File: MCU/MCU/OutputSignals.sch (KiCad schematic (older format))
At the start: 31 parts, among them J11 Conn_01x02, J12 Conn_01x02, J13 Conn_01x02, Q2 8050, Q3 8050, Q4 8550, Q5 8050, U10 LMV321, U11 PC817, U9 ICL7660

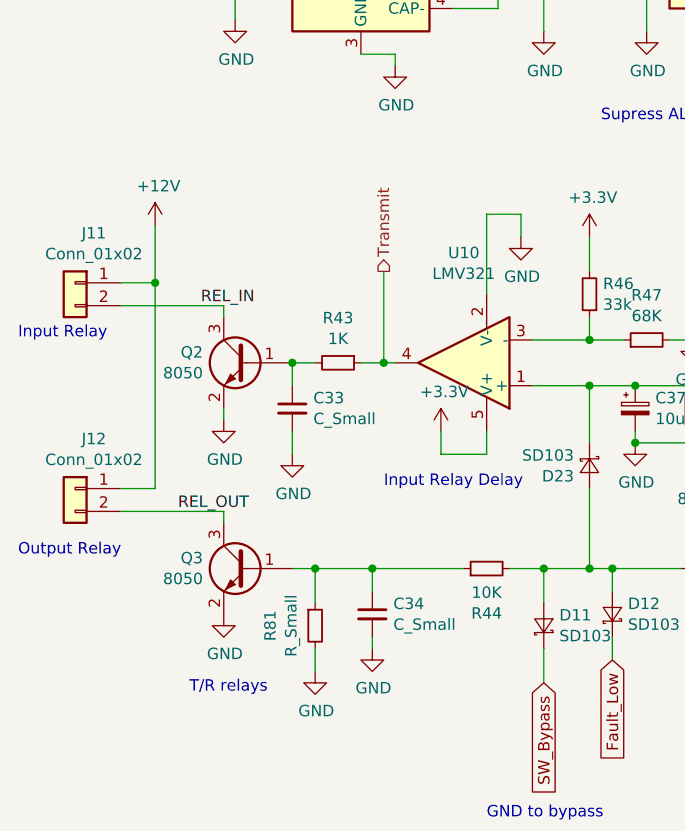
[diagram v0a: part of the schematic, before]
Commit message: OPA1000 and 2000 compatibility
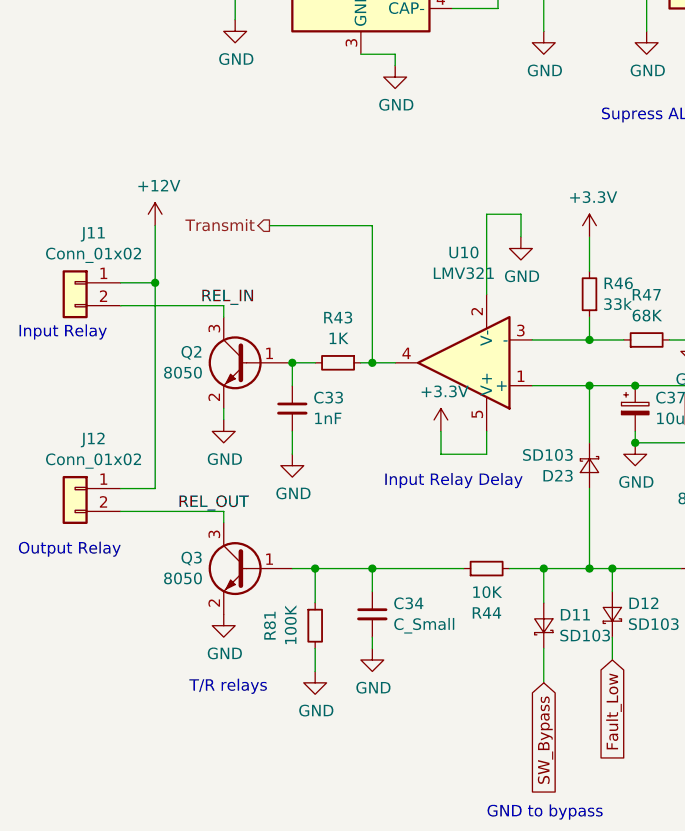
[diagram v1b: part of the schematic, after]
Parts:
- C33: value C_Small -> 1nF
- R81: value R_Small -> 100K
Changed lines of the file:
@@
 EESchema Schematic File Version 4
-LIBS:MCU-cache
 EELAYER 30 0
 EELAYER END
@@
 Text HLabel 4900 2450 3    50   Input ~ 0
 ALC_trig
-Text HLabel 2850 2850 1    50   Output ~ 0
-Transmit
 Text Notes 1250 4100 0    50   ~ 0
 Output Relay
@@
 	4100 3150 4200 3150
 Wire Wire Line
-	2850 2850 2850 3250
-Wire Wire Line
-	2850 3250 2900 3250
-Wire Wire Line
 	2450 4150 2550 4150
 Wire Wire Line
@@
 $EndComp
 Wire Wire Line
-	2750 3250 2850 3250
-Connection ~ 2850 3250
-Wire Wire Line
 	2550 3250 2450 3250
 $Comp
@@
 P 2450 3450
 F 0 "C33" H 2542 3496 50  0000 L CNN
-F 1 "C_Small" H 2542 3405 50  0000 L CNN
+F 1 "1nF" H 2542 3405 50  0000 L CNN
 F 2 "Capacitors_SMD:C_0805" H 2450 3450 50  0001 C CNN
 F 3 "~" H 2450 3450 50  0001 C CNN
@@
 P 2550 4400
 F 0 "R81" V 2354 4400 50  0000 C CNN
-F 1 "R_Small" V 2445 4400 50  0000 C CNN
+F 1 "100K" V 2445 4400 50  0000 C CNN
 F 2 "Resistors_SMD:R_0805" H 2550 4400 50  0001 C CNN
 F 3 "~" H 2550 4400 50  0001 C CNN
@@
 Text Notes 4800 3350 0    50   ~ 0
 Add a diode between C37 and PTT to discharge
+Text HLabel 2350 2650 0    50   Output ~ 0
+Transmit
+Wire Wire Line
+	2750 3250 2800 3250
+Wire Wire Line
+	2800 2650 2800 3250
+Wire Wire Line
+	2350 2650 2800 2650
+Connection ~ 2800 3250
+Wire Wire Line
+	2800 3250 2900 3250
 $EndSCHEMATC
